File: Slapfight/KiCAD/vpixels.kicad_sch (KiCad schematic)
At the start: 15 parts, among them U7B_ 74LS02, U7C_ 74LS00, U8A_ 74LS74, U8B 82S129 - ROM15, U8C 74LS163, U8D_ 74LS86, U8E 74LS283, U8H 74LS374, U9B 74LS163, U9C 74LS163, U9D_ 74LS86, U9E 74LS283, U9H_ 74LS74, U9M_ 74LS14, U9N_ 74LS14

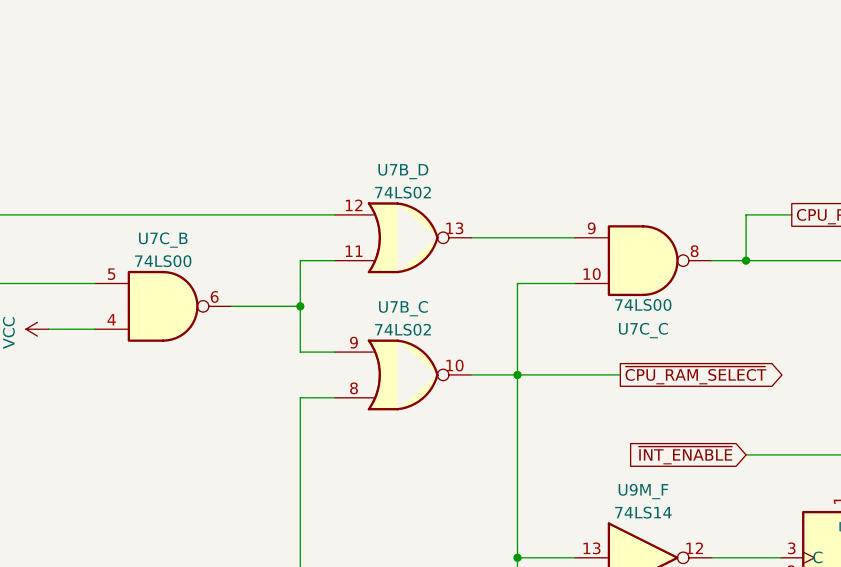
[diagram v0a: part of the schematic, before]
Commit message: Component naming updates
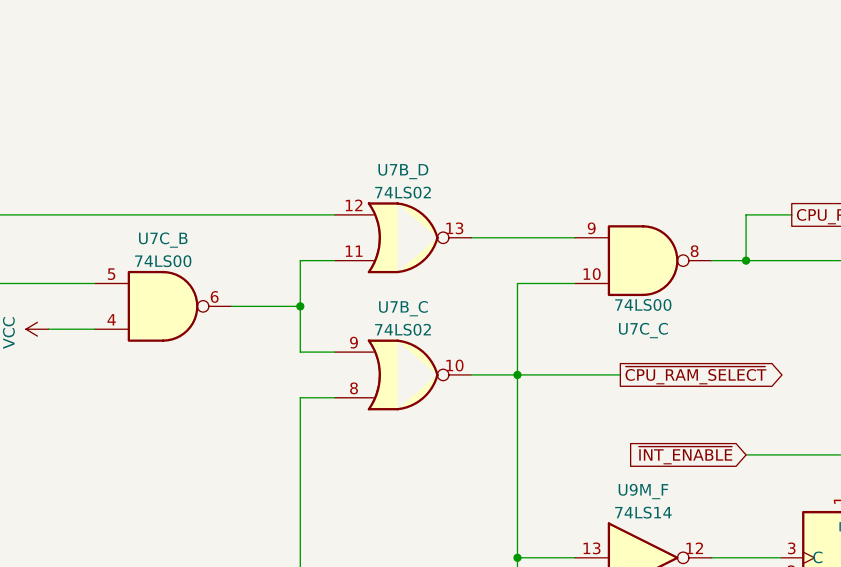
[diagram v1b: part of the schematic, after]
